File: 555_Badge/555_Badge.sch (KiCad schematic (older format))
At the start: 13 parts

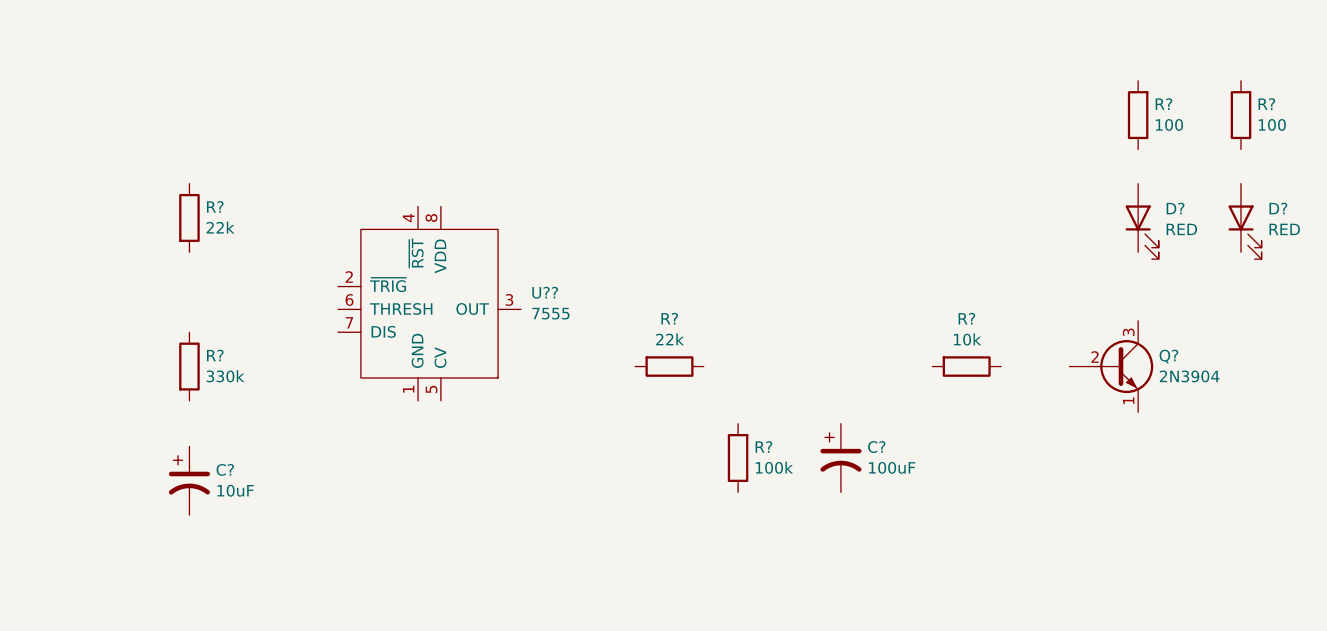
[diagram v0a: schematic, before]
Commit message: Added libraries folder and finished 555 schematic
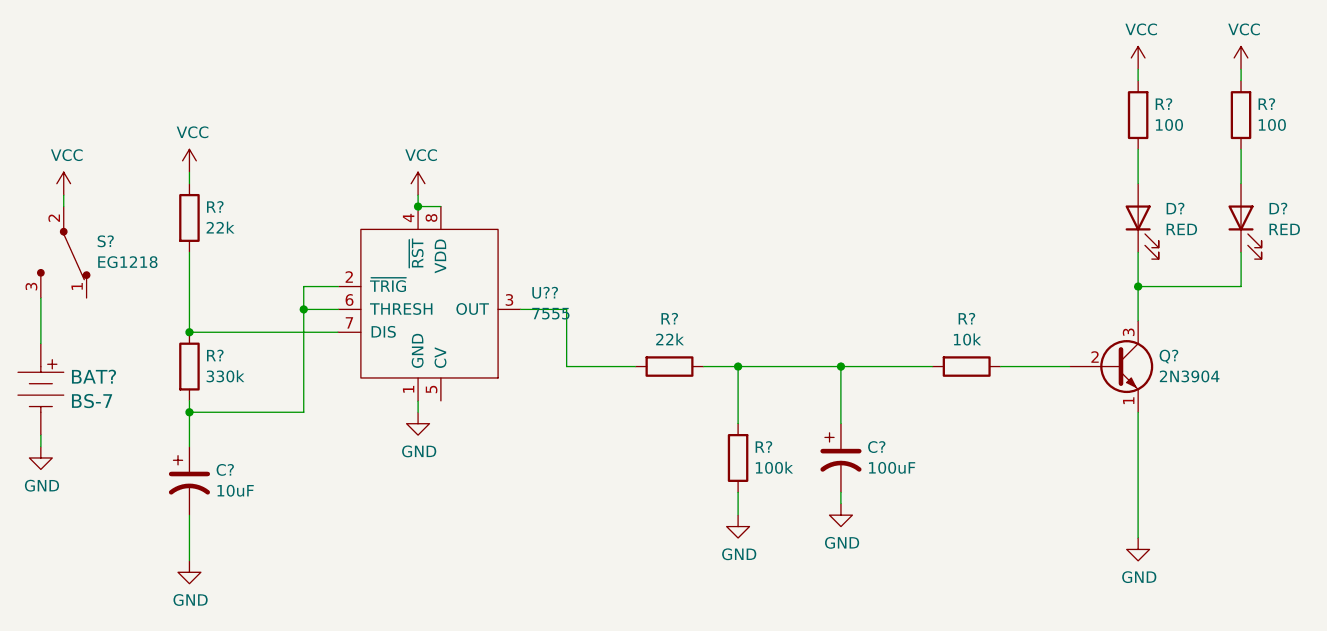
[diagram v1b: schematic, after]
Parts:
- added BAT?: BS-7, digikey-footprints:Battery_Holder_Coin_2032_BS-7, symbol dk_Battery-Holders-Clips-Contacts:BS-7
- added S?: EG1218, digikey-footprints:Switch_Slide_11.6x4mm_EG1218, symbol dk_Slide-Switches:EG1218
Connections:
- net GND: now reaches U??.1 (GND)
- net GND: now also C?.2, C?.2, Q?.1 (E), R?.1, BAT?.Neg
- net at U??.2 (~TRIG): now also C?.1, R?.2, U??.6 (THRESH)
- net at U??.3 (OUT): now also R?.2
- net VCC: now reaches U??.4 (~RST)
- net VCC: now also R?.1, R?.2, R?.2, U??.8 (VDD), S?.2
- net at U??.7 (DIS): now also R?.1, R?.2
- net at R?.1: now also C?.1, R?.2, R?.2
- net at R?.1: now also D?.2 (A) (x2)
- net at R?.1: now also Q?.2 (B)
- net at D?.1 (K): now also D?.1 (K), Q?.3 (C)
- new net: BAT?.Pos, S?.3

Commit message: Assigned footprints to symbols
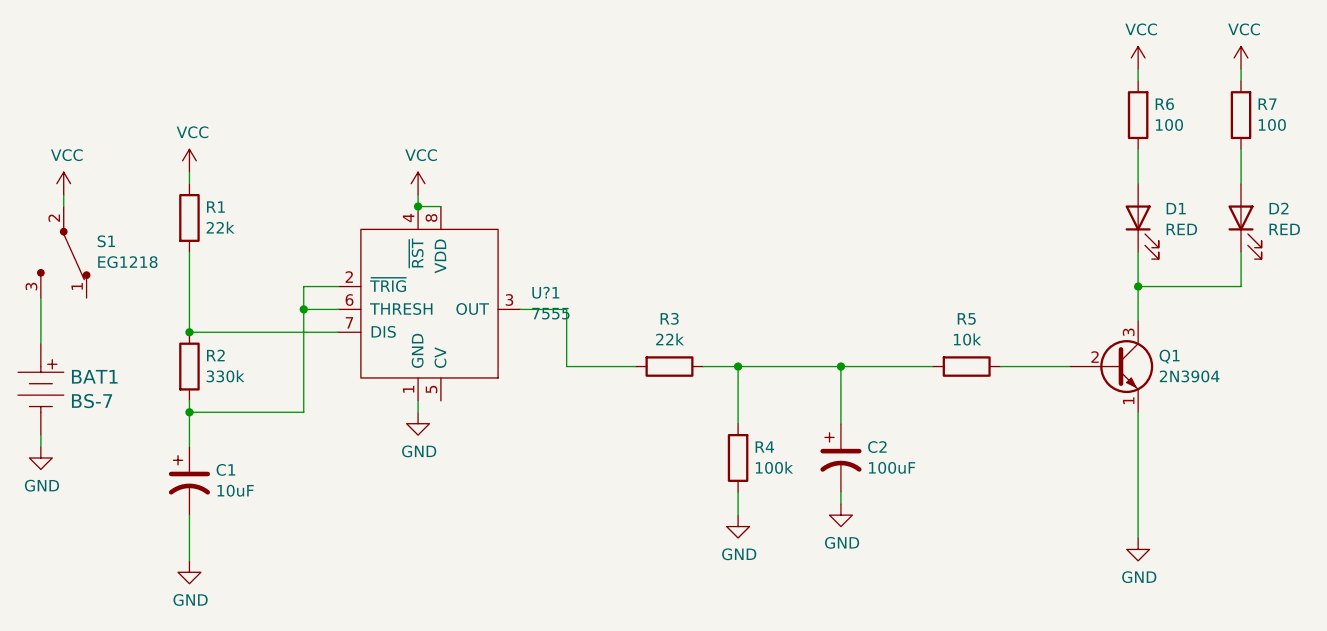
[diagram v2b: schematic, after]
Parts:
- C1: renamed from C?; footprint (none) -> Capacitor_THT:CP_Radial_D5.0mm_P2.00mm
- C2: renamed from C?; footprint (none) -> Capacitor_THT:CP_Radial_D6.3mm_P2.50mm
- D1, D2: renamed from D?; footprint (none) -> LED_THT:LED_D3.0mm
- Q1: renamed from Q?; footprint Package_TO_SOT_THT:TO-92_Inline -> digikey-footprints:TO-92-3
- R1, R2, R3, R4, R5, R6, R7: renamed from R?; footprint (none) -> Resistor_THT:R_Axial_DIN0207_L6.3mm_D2.5mm_P7.62mm_Horizontal
- U?1: renamed from U??; footprint (none) -> 555_Badge:ICM7555-PDIP
- gave numbers to parts that had none: 2
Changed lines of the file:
@@
 $EndDescr
 $Comp
-L 555_badge:7555 U??
+L 555_badge:7555 U?1
 U 1 1 61C28550
 P 4850 4500
-F 0 "U??" H 5294 4571 50  0000 L CNN
+F 0 "U?1" H 5294 4571 50  0000 L CNN
 F 1 "7555" H 5294 4480 50  0000 L CNN
-F 2 "" H 4850 4500 50  0001 C CNN
+F 2 "555_Badge:ICM7555-PDIP" H 4850 4500 50  0001 C CNN
 F 3 "" H 4850 4500 50  0001 C CNN
 	1    4850 4500
@@
 $EndComp
 $Comp
-L Device:R R?
+L Device:R R1
 U 1 1 61C2931F
 P 3800 4100
-F 0 "R?" H 3870 4146 50  0000 L CNN
+F 0 "R1" H 3870 4146 50  0000 L CNN
 F 1 "22k" H 3870 4055 50  0000 L CNN
-F 2 "" V 3730 4100 50  0001 C CNN
+F 2 "Resistor_THT:R_Axial_DIN0207_L6.3mm_D2.5mm_P7.62mm_Horizontal" V 3730 4100 50  0001 C CNN
 F 3 "~" H 3800 4100 50  0001 C CNN
 	1    3800 4100
@@
 $EndComp
 $Comp
-L Device:R R?
+L Device:R R2
 U 1 1 61C29885
 P 3800 4750
-F 0 "R?" H 3870 4796 50  0000 L CNN
+F 0 "R2" H 3870 4796 50  0000 L CNN
 F 1 "330k" H 3870 4705 50  0000 L CNN
-F 2 "" V 3730 4750 50  0001 C CNN
+F 2 "Resistor_THT:R_Axial_DIN0207_L6.3mm_D2.5mm_P7.62mm_Horizontal" V 3730 4750 50  0001 C CNN
 F 3 "~" H 3800 4750 50  0001 C CNN
 	1    3800 4750
@@
 $EndComp
 $Comp
-L Device:R R?
+L Device:R R3
 U 1 1 61C29AC3
 P 5900 4750
-F 0 "R?" V 5693 4750 50  0000 C CNN
+F 0 "R3" V 5693 4750 50  0000 C CNN
 F 1 "22k" V 5784 4750 50  0000 C CNN
-F 2 "" V 5830 4750 50  0001 C CNN
+F 2 "Resistor_THT:R_Axial_DIN0207_L6.3mm_D2.5mm_P7.62mm_Horizontal" V 5830 4750 50  0001 C CNN
 F 3 "~" H 5900 4750 50  0001 C CNN
 	1    5900 4750
@@
 $EndComp
 $Comp
-L Device:R R?
+L Device:R R4
 U 1 1 61C2A1F6
 P 6200 5150
-F 0 "R?" H 6130 5104 50  0000 R CNN
+F 0 "R4" H 6130 5104 50  0000 R CNN
 F 1 "100k" H 6130 5195 50  0000 R CNN
-F 2 "" V 6130 5150 50  0001 C CNN
+F 2 "Resistor_THT:R_Axial_DIN0207_L6.3mm_D2.5mm_P7.62mm_Horizontal" V 6130 5150 50  0001 C CNN
 F 3 "~" H 6200 5150 50  0001 C CNN
 	1    6200 5150
@@
 $EndComp
 $Comp
-L Device:R R?
+L Device:R R6
 U 1 1 61C2A680
 P 7950 3650
-F 0 "R?" H 7880 3604 50  0000 R CNN
+F 0 "R6" H 7880 3604 50  0000 R CNN
 F 1 "100" H 7880 3695 50  0000 R CNN
-F 2 "" V 7880 3650 50  0001 C CNN
+F 2 "Resistor_THT:R_Axial_DIN0207_L6.3mm_D2.5mm_P7.62mm_Horizontal" V 7880 3650 50  0001 C CNN
 F 3 "~" H 7950 3650 50  0001 C CNN
 	1    7950 3650
@@
 $EndComp
 $Comp
-L Device:R R?
+L Device:R R7
 U 1 1 61C2ACEE
 P 8400 3650
-F 0 "R?" H 8330 3604 50  0000 R CNN
+F 0 "R7" H 8330 3604 50  0000 R CNN
 F 1 "100" H 8330 3695 50  0000 R CNN
-F 2 "" V 8330 3650 50  0001 C CNN
+F 2 "Resistor_THT:R_Axial_DIN0207_L6.3mm_D2.5mm_P7.62mm_Horizontal" V 8330 3650 50  0001 C CNN
 F 3 "~" H 8400 3650 50  0001 C CNN
 	1    8400 3650
@@
 $EndComp
 $Comp
-L Device:R R?
+L Device:R R5
 U 1 1 61C2AFCA
 P 7200 4750
-F 0 "R?" V 6993 4750 50  0000 C CNN
+F 0 "R5" V 6993 4750 50  0000 C CNN
 F 1 "10k" V 7084 4750 50  0000 C CNN
-F 2 "" V 7130 4750 50  0001 C CNN
+F 2 "Resistor_THT:R_Axial_DIN0207_L6.3mm_D2.5mm_P7.62mm_Horizontal" V 7130 4750 50  0001 C CNN
 F 3 "~" H 7200 4750 50  0001 C CNN
 	1    7200 4750
@@
 $EndComp
 $Comp
-L Device:CP1 C?
+L Device:CP1 C2
 U 1 1 61C2CD88
 P 6650 5150
-F 0 "C?" H 6765 5196 50  0000 L CNN
+F 0 "C2" H 6765 5196 50  0000 L CNN
 F 1 "100uF" H 6765 5105 50  0000 L CNN
-F 2 "" H 6650 5150 50  0001 C CNN
+F 2 "Capacitor_THT:CP_Radial_D6.3mm_P2.50mm" H 6650 5150 50  0001 C CNN
 F 3 "~" H 6650 5150 50  0001 C CNN
 	1    6650 5150
@@
 $EndComp
 $Comp
-L Device:CP1 C?
+L Device:CP1 C1
 U 1 1 61C2DD86
 P 3800 5250
-F 0 "C?" H 3915 5296 50  0000 L CNN
+F 0 "C1" H 3915 5296 50  0000 L CNN
 F 1 "10uF" H 3915 5205 50  0000 L CNN
-F 2 "" H 3800 5250 50  0001 C CNN
+F 2 "Capacitor_THT:CP_Radial_D5.0mm_P2.00mm" H 3800 5250 50  0001 C CNN
 F 3 "~" H 3800 5250 50  0001 C CNN
 	1    3800 5250
@@
 $EndComp
 $Comp
-L Device:LED D?
+L Device:LED D1
 U 1 1 61C2E9FE
 P 7950 4100
-F 0 "D?" V 7989 3982 50  0000 R CNN
+F 0 "D1" V 7989 3982 50  0000 R CNN
 F 1 "RED" V 7898 3982 50  0000 R CNN
-F 2 "" H 7950 4100 50  0001 C CNN
+F 2 "LED_THT:LED_D3.0mm" H 7950 4100 50  0001 C CNN
 F 3 "~" H 7950 4100 50  0001 C CNN
 	1    7950 4100
@@
 $EndComp
 $Comp
-L Device:LED D?
+L Device:LED D2
 U 1 1 61C2F738
 P 8400 4100
-F 0 "D?" V 8439 3982 50  0000 R CNN
+F 0 "D2" V 8439 3982 50  0000 R CNN
 F 1 "RED" V 8348 3982 50  0000 R CNN
-F 2 "" H 8400 4100 50  0001 C CNN
+F 2 "LED_THT:LED_D3.0mm" H 8400 4100 50  0001 C CNN
 F 3 "~" H 8400 4100 50  0001 C CNN
 	1    8400 4100
@@
 $EndComp
 $Comp
-L Transistor_BJT:2N3904 Q?
+L Transistor_BJT:2N3904 Q1
 U 1 1 61C30386
 P 7850 4750
-F 0 "Q?" H 8040 4796 50  0000 L CNN
+F 0 "Q1" H 8040 4796 50  0000 L CNN
 F 1 "2N3904" H 8040 4705 50  0000 L CNN
-F 2 "Package_TO_SOT_THT:TO-92_Inline" H 8050 4675 50  0001 L CIN
+F 2 "digikey-footprints:TO-92-3" H 8050 4675 50  0001 L CIN
 F 3 "https://www.onsemi.com/pub/Collateral/2N3903-D.PDF" H 7850 4750 50  0001 L CNN
 	1    7850 4750
@@
 $EndComp
 $Comp
-L dk_Battery-Holders-Clips-Contacts:BS-7 BAT?
+L dk_Battery-Holders-Clips-Contacts:BS-7 BAT1
 U 1 1 61C2ADBE
 P 3150 4850
-F 0 "BAT?" H 3278 4903 60  0000 L CNN
+F 0 "BAT1" H 3278 4903 60  0000 L CNN
 F 1 "BS-7" H 3278 4797 60  0000 L CNN
 F 2 "digikey-footprints:Battery_Holder_Coin_2032_BS-7" H 3350 5050 60  0001 L CNN
@@
 $EndComp
 $Comp
-L dk_Slide-Switches:EG1218 S?
+L dk_Slide-Switches:EG1218 S1
 U 1 1 61C2BE1E
 P 3250 4250
-F 0 "S?" V 3204 4394 50  0000 L CNN
+F 0 "S1" V 3204 4394 50  0000 L CNN
 F 1 "EG1218" V 3295 4394 50  0000 L CNN
 F 2 "digikey-footprints:Switch_Slide_11.6x4mm_EG1218" H 3450 4450 50  0001 L CNN
@@
 $EndComp
 $Comp
-L power:GND #PWR?
+L power:GND #PWR04
 U 1 1 61C2E667
 P 3800 5600
-F 0 "#PWR?" H 3800 5350 50  0001 C CNN
+F 0 "#PWR04" H 3800 5350 50  0001 C CNN
 F 1 "GND" H 3805 5427 50  0000 C CNN
 F 2 "" H 3800 5600 50  0001 C CNN
@@
 $EndComp
 $Comp
-L power:GND #PWR?
+L power:GND #PWR01
 U 1 1 61C2E92B
 P 3150 5100
-F 0 "#PWR?" H 3150 4850 50  0001 C CNN
+F 0 "#PWR01" H 3150 4850 50  0001 C CNN
 F 1 "GND" H 3155 4927 50  0000 C CNN
 F 2 "" H 3150 5100 50  0001 C CNN
@@
 $EndComp
 $Comp
-L power:GND #PWR?
+L power:GND #PWR07
 U 1 1 61C2F06D
 P 6200 5400
-F 0 "#PWR?" H 6200 5150 50  0001 C CNN
+F 0 "#PWR07" H 6200 5150 50  0001 C CNN
 F 1 "GND" H 6205 5227 50  0000 C CNN
 F 2 "" H 6200 5400 50  0001 C CNN
@@
 $EndComp
 $Comp
-L power:GND #PWR?
+L power:GND #PWR08
 U 1 1 61C2F82D
 P 6650 5350
-F 0 "#PWR?" H 6650 5100 50  0001 C CNN
+F 0 "#PWR08" H 6650 5100 50  0001 C CNN
 F 1 "GND" H 6655 5177 50  0000 C CNN
 F 2 "" H 6650 5350 50  0001 C CNN
@@
 $EndComp
 $Comp
-L power:GND #PWR?
+L power:GND #PWR010
 U 1 1 61C2FAD0
 P 7950 5500
-F 0 "#PWR?" H 7950 5250 50  0001 C CNN
+F 0 "#PWR010" H 7950 5250 50  0001 C CNN
 F 1 "GND" H 7955 5327 50  0000 C CNN
 F 2 "" H 7950 5500 50  0001 C CNN
@@
 $EndComp
 $Comp
-L power:VCC #PWR?
+L power:VCC #PWR02
 U 1 1 61C30034
 P 3250 4000
-F 0 "#PWR?" H 3250 3850 50  0001 C CNN
+F 0 "#PWR02" H 3250 3850 50  0001 C CNN
 F 1 "VCC" H 3265 4173 50  0000 C CNN
 F 2 "" H 3250 4000 50  0001 C CNN
@@
 $EndComp
 $Comp
-L power:VCC #PWR?
+L power:VCC #PWR03
 U 1 1 61C3089C
 P 3800 3900
-F 0 "#PWR?" H 3800 3750 50  0001 C CNN
+F 0 "#PWR03" H 3800 3750 50  0001 C CNN
 F 1 "VCC" H 3815 4073 50  0000 C CNN
 F 2 "" H 3800 3900 50  0001 C CNN
@@
 $EndComp
 $Comp
-L power:VCC #PWR?
+L power:VCC #PWR05
 U 1 1 61C30F90
 P 4800 4000
-F 0 "#PWR?" H 4800 3850 50  0001 C CNN
+F 0 "#PWR05" H 4800 3850 50  0001 C CNN
 F 1 "VCC" H 4815 4173 50  0000 C CNN
 F 2 "" H 4800 4000 50  0001 C CNN
@@
 $EndComp
 $Comp
-L power:VCC #PWR?
+L power:VCC #PWR09
 U 1 1 61C31262
 P 7950 3450
-F 0 "#PWR?" H 7950 3300 50  0001 C CNN
+F 0 "#PWR09" H 7950 3300 50  0001 C CNN
 F 1 "VCC" H 7965 3623 50  0000 C CNN
 F 2 "" H 7950 3450 50  0001 C CNN
@@
 $EndComp
 $Comp
-L power:VCC #PWR?
+L power:VCC #PWR011
 U 1 1 61C3201A
 P 8400 3450
-F 0 "#PWR?" H 8400 3300 50  0001 C CNN
+F 0 "#PWR011" H 8400 3300 50  0001 C CNN
 F 1 "VCC" H 8415 3623 50  0000 C CNN
 F 2 "" H 8400 3450 50  0001 C CNN
@@
 	8400 3450 8400 3500
 $Comp
-L power:GND #PWR?
+L power:GND #PWR06
 U 1 1 61C3AB09
 P 4800 4950
-F 0 "#PWR?" H 4800 4700 50  0001 C CNN
+F 0 "#PWR06" H 4800 4700 50  0001 C CNN
 F 1 "GND" H 4805 4777 50  0000 C CNN
 F 2 "" H 4800 4950 50  0001 C CNN
